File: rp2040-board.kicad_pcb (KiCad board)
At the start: 4 copper layers, 105.3 x 75.1 mm, 178 parts, among them J1 24V IN, J10 E0-RUNOUT, J11 FAN0, J12 FAN1, J13 FAN2, J14 HB, J15 E0, J16 TH-E0, J17 X-STEPPER, J18 Y-STEPPER, J19 ZA-STEPPER, J2 USB4105-GF-A, J20 E0-STEPPER, J21 ZB-STEPPER, J22 Exp. Header 2, J23 Exp. Header 3, J4 Exp. Header 1, J5 PROBE, J6 X-ENDSTOP, J7 TH-HB, J8 Y-ENDSTOP, J9 Z-ENDSTOP, Q1 AO3400C, Q2 AO3400C, Q3 AO3400C, U1 AMS1117-3.3, U10 RP2040, U11 W25Q80DVSNIG, U2 TPS5450DDAR, U3 74HCT365D,653, U4 FDS8896, U5 FDS8896, U6 TMC2226-SA-T, U7 TMC2226-SA-T, U8 TMC2226-SA-T, U9 TMC2226-SA-T, Y1 12MHz

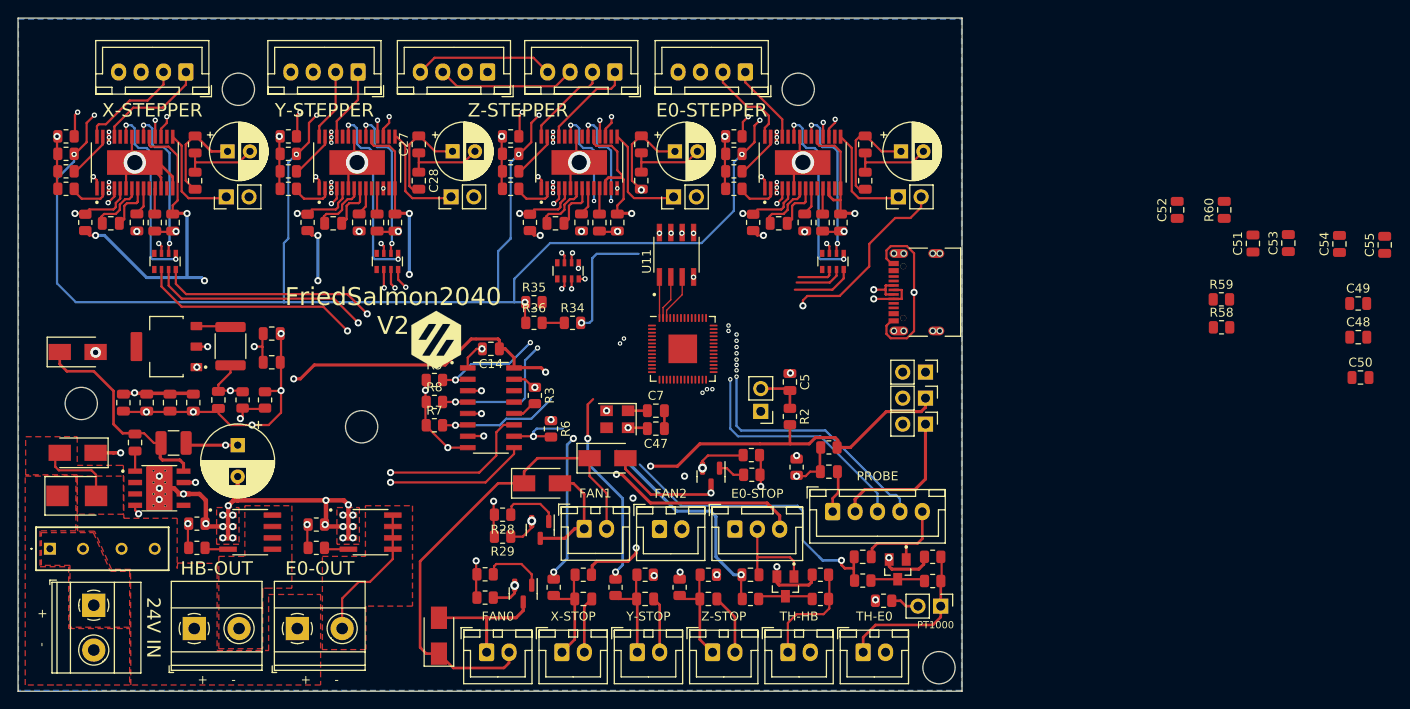
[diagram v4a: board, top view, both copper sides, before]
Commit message: Updates, Move to 0602, Optimize Routing
* 0805 -> 0602
* Flash 8MB SOIC8 -> Flash 16MB USON 2x3
* Indev Pic
* Trace Optimization
* Whatever else i forgor
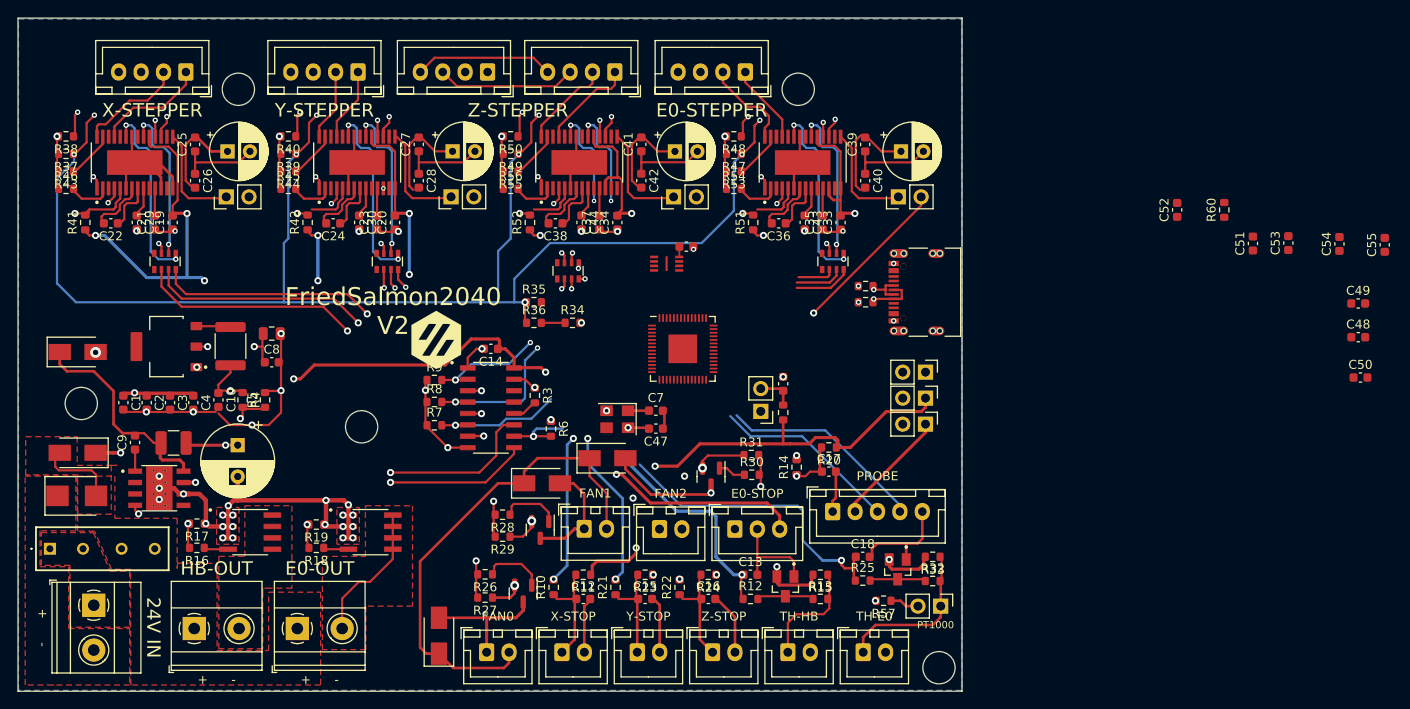
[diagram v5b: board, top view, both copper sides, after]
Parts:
- added C56: 0.1uF, Capacitor_SMD:C_0603_1608Metric, F.Cu at (172.2, 88.5)
- C1, C10, C12, C13, C14, C15, C16, C17, C18, C19, C2, C20, C21, C22, C23, C24, C25, C26, C27, C28, C29, C3, C30, C33, C34, C35, C36, C37, C38, C39, C4, C40, C41, C42, C43, C44, C47, C48, C49, C5, C50, C51, C52, C53, C54, C55, C7, C8, C9: footprint Capacitor_SMD:C_0805_2012Metric -> Capacitor_SMD:C_0603_1608Metric
- R10, R11, R12, R13, R14, R15, R16, R17, R18, R19, R2, R20, R21, R22, R23, R24, R25, R26, R27, R28, R29, R3, R30, R31, R32, R33, R34, R35, R36, R37, R38, R39, R4, R40, R41, R42, R43, R44, R45, R46, R47, R48, R49, R5, R50, R51, R52, R53, R54, R55, R56, R57, R58, R59, R6, R7, R8, R9: footprint Resistor_SMD:R_0805_2012Metric -> Resistor_SMD:R_0603_1608Metric
- R60: footprint Capacitor_SMD:C_0805_2012Metric -> Resistor_SMD:R_0603_1608Metric
- U11: value W25Q80DVSNIG -> W25Q16JVUXIQ; footprint FDS8896:SOIC127P600X175-8N -> W25Q16JVUXIQ:SON50P300X200X60-9N
- moved R58 40.0 mm to (192.2, 92.9)
- moved R59 39.7 mm to (192.2, 94.7)
- moved U11 1.49 mm to (170.0, 90.4), turned to 0 degrees
- moved R2 0.87 mm to (183.0, 107.0)
- moved C5 0.78 mm to (183.0, 103.8)
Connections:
- net /E0_PWM renamed E0_PWM
- net /E0_THERM renamed E0_THERM
- net /FAN0_PWM renamed FAN0_PWM
- net /FAN1_PWM renamed FAN1_PWM
- net /FAN2_PWM renamed FAN2_PWM
- net /HB_PWM renamed HB_PWM
- net /HB_THERM renamed HB_THERM
- net Net-(R16-Pad2) renamed HB
- net Net-(R18-Pad2) renamed E0
- net Net-(R26-Pad2) renamed FAN0
- net Net-(R28-Pad2) renamed FAN1
- net Net-(R30-Pad2) renamed FAN2
- C25 pad 1: Net-(C25-Pad1) -> GND
- C26 pad 1: Net-(C25-Pad1) -> GND
- C27 pad 1: Net-(C27-Pad1) -> GND
- C28 pad 1: Net-(C27-Pad1) -> GND
- C31 pad 2: Net-(C25-Pad1) -> GND
- C32 pad 2: Net-(C27-Pad1) -> GND
- C39 pad 1: Net-(C39-Pad1) -> GND
- C40 pad 1: Net-(C39-Pad1) -> GND
- C41 pad 1: Net-(C41-Pad1) -> GND
- C42 pad 1: Net-(C41-Pad1) -> GND
- C45 pad 2: Net-(C39-Pad1) -> GND
- C46 pad 2: Net-(C41-Pad1) -> GND
- C48 pad 1: Net-(C48-Pad1) -> +3.3V
- C49 pad 1: Net-(C48-Pad1) -> +3.3V
- C50 pad 1: Net-(C48-Pad1) -> +3.3V
- D2 pad 1: Net-(D2-Pad1) -> GND
- J1 pad 2: Net-(D2-Pad1) -> GND
- J5 pad 3: /PROBE_SRVO -> PROBE_DET
- J5 pad 4: /PROBE_DET -> PROBE_SRV
- RN2 pad 5: unconnected-(RN2-Pad5) -> YSTP
- U10 pad 19: unconnected-(U10-Pad19) -> GND
- U10 pad 23: Net-(C48-Pad1) -> +3.3V
- U10 pad 25: unconnected-(U10-Pad24) -> unconnected-(U10-Pad25)
- U10 pad 29: /PROBE_SRVO -> PROBE_SRV
- U10 pad 30: /PROBE_DET -> PROBE_DET
- U10 pad 45: Net-(C48-Pad1) -> +3.3V
- U10 pad 50: Net-(C48-Pad1) -> +3.3V
- U11 pad 8: VCC -> Net-(U11-Pad8)
- U2 pad 2: (no net) -> unconnected-(U2-Pad2)
- U2 pad 3: (no net) -> unconnected-(U2-Pad3)
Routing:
- net /PROBE_DET: track 28.5 -> 0.00 mm, vias 1 -> 0
- net /PROBE_SRVO: track 26.9 -> 0.00 mm, vias 1 -> 0
- net unconnected-(RN2-Pad5): track 25.8 -> 0.00 mm, vias 1 -> 0
- net YSTP: track 0.00 -> 25.8 mm, vias 0 -> 1
- net GPIO27: track 23.6 -> 0.00 mm, vias 1 -> 0
- net PROBE_SRV: track 0.00 -> 23.1 mm
- net GPIO25: track 20.9 -> 0.03 mm, vias 1 -> 0
- net PROBE_DET: track 0.00 -> 20.8 mm
- net GPIO26: track 20.0 -> 0.00 mm, vias 1 -> 0
- net ZDIR: track 18.6 -> 0.70 mm
- net GND: track 228.1 -> 243.6 mm, vias 55 -> 50
- net UART_TX: track 13.6 -> 0.00 mm
- net Net-(C39-Pad1): track 9.01 -> 0.00 mm
- net Net-(C41-Pad1): track 8.73 -> 0.00 mm
- net Net-(C27-Pad1): track 8.70 -> 0.00 mm
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- added copper zone on B.Cu, net GND
- added copper zone on In1.Cu, net GND
- added copper zone on In2.Cu, net GND
- removed copper zone on B.Cu, net Net-(D2-Pad1)
- removed copper zone on F.Cu, net Net-(D2-Pad1)
- removed copper zone on In1.Cu, net Net-(D2-Pad1)
- removed copper zone on In2.Cu, net Net-(D2-Pad1)
